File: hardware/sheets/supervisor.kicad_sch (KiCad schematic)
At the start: 20 parts, among them J1 QSPI_FLASH, J2 USB_HOST, J3 POST_HEX, J4 CONSOLE, J5 SWD, U1 RP2040, Y1 12MHz

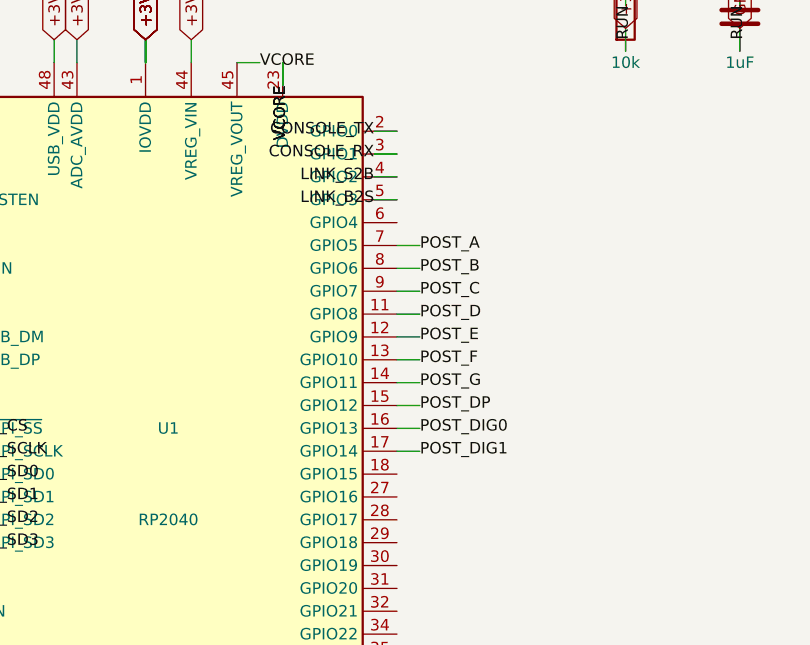
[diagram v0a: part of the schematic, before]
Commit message: Fix all medium design-review findings (M1-M8)
- M1: Supervisor link moved to GPIO4/5 (real UART1 pair); POST -> GPIO6-15
- M2: CNT_RUN = LD0.LD1.LD2 gates every '163 CEP (load-cascade hazard)
- M3: ~WR / IO-M pruned to cpu_core-internal; DRQ2/3 pulled + noted;
  doc S5.2 "as built: 48/48" + S16 updated
- M4: true XT-IDE rev-2 map (A0<->A3 swap): data 0x300, latch 0x301,
  CS1 0x307/0x30F, drive DA0 = bus A3 - matches XTIDE UB "rev 2" type
- M5: COM4 -> bus IRQ2 line (IRQ9 via AT redirect); IRQ10/11/14/15 marked
  off-header; ~REFRESH added to mxbus ISA_CTRL; questions-sidecar superseded
- M6: card_isatest clock tree on unswitched V5RAW (spec S8)
- M7: card_isatest IRQ2-8/DRQ1-3 idle pull-downs (spec S4/S9)
- M8: com_port JP1 selects 16550 RX source (DB9 vs TTL console); 5V note

Rebuilt motherboard + cards; structural ERC = 0; netlist-verified.
Fix log in hardware/notes/design-review-2026-07-03.md (batch 3).

Co-Authored-By: Claude Fable 5 <noreply@anthropic.com>
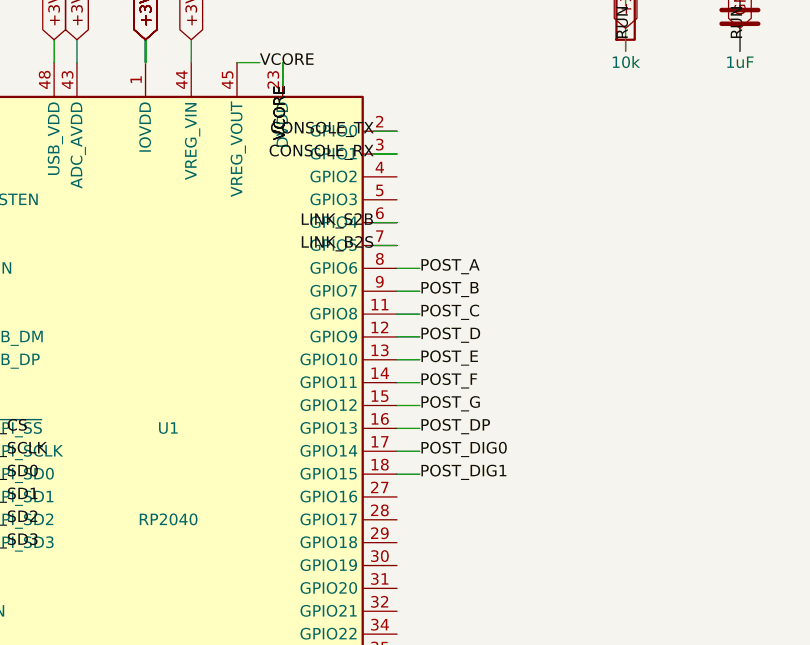
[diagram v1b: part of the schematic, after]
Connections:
- net LINK_B2S: now also U1.7 (GPIO5); no longer U1.5 (GPIO3)
- net LINK_S2B: now also U1.6 (GPIO4); no longer U1.4 (GPIO2)
- net POST_A: now also U1.8 (GPIO6); no longer U1.7 (GPIO5)
- net POST_B: now also U1.9 (GPIO7); no longer U1.8 (GPIO6)
- net POST_C: now also U1.11 (GPIO8); no longer U1.9 (GPIO7)
- net POST_D: now also U1.12 (GPIO9); no longer U1.11 (GPIO8)
- net POST_DIG0: now also U1.17 (GPIO14); no longer U1.16 (GPIO13)
- net POST_DIG1: now also U1.18 (GPIO15); no longer U1.17 (GPIO14)
- net POST_DP: now also U1.16 (GPIO13); no longer U1.15 (GPIO12)
- net POST_E: now also U1.13 (GPIO10); no longer U1.12 (GPIO9)
- net POST_F: now also U1.14 (GPIO11); no longer U1.13 (GPIO10)
- net POST_G: now also U1.15 (GPIO12); no longer U1.14 (GPIO11)
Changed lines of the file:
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@@
-	(wire
-		(pts
-			(xy 203.2 101.6)
-			(xy 205.74 101.6)
-		)
-		(stroke
-			(width 0)
-			(type default)
-		)
-	)
-	(label "POST_A"
-		(at 205.74 101.6 0)
-		(effects
-			(font
-				(size 1.27 1.27)
-			)
-		)
-	)
 	(wire
 		(pts
@@
 		)
 	)
-	(label "POST_B"
+	(label "POST_A"
 		(at 205.74 104.14 0)
 		(effects
@@
 		)
 	)
-	(label "POST_C"
+	(label "POST_B"
 		(at 205.74 106.68 0)
 		(effects
@@
 		)
 	)
-	(label "POST_D"
+	(label "POST_C"
 		(at 205.74 109.22 0)
 		(effects
@@
 		)
 	)
-	(label "POST_E"
+	(label "POST_D"
 		(at 205.74 111.76 0)
 		(effects
@@
 		)
 	)
-	(label "POST_F"
+	(label "POST_E"
 		(at 205.74 114.3 0)
 		(effects
@@
 		)
 	)
-	(label "POST_G"
+	(label "POST_F"
 		(at 205.74 116.84 0)
 		(effects
@@
 		)
 	)
-	(label "POST_DP"
+	(label "POST_G"
 		(at 205.74 119.38 0)
 		(effects
@@
 		)
 	)
-	(label "POST_DIG0"
+	(label "POST_DP"
 		(at 205.74 121.92 0)
 		(effects
@@
 		)
 	)
+	(label "POST_DIG0"
+		(at 205.74 124.46 0)
+		(effects
+			(font
+				(size 1.27 1.27)
+			)
+		)
+	)
+	(wire
+		(pts
+			(xy 203.2 127)
+			(xy 205.74 127)
+		)
+		(stroke
+			(width 0)
+			(type default)
+		)
+	)
 	(label "POST_DIG1"
-		(at 205.74 124.46 0)
+		(at 205.74 127 0)
 		(effects
 			(font
@@
 	(wire
 		(pts
-			(xy 203.2 93.98)
-			(xy 200.66 93.98)
+			(xy 203.2 99.06)
+			(xy 200.66 99.06)
 		)
 		(stroke
@@
 	)
 	(label "LINK_S2B"
-		(at 200.66 93.98 180)
-		(effects
-			(font
-				(size 1.27 1.27)
-			)
-		)
-	)
-	(wire
-		(pts
-			(xy 203.2 96.52)
-			(xy 200.66 96.52)
+		(at 200.66 99.06 180)
+		(effects
+			(font
+				(size 1.27 1.27)
+			)
+		)
+	)
+	(wire
+		(pts
+			(xy 203.2 101.6)
+			(xy 200.66 101.6)
 		)
 		(stroke
@@
 	)
 	(label "LINK_B2S"
-		(at 200.66 96.52 180)
+		(at 200.66 101.6 180)
 		(effects
 			(font
@@
 		(instances
 			(project "mini-xt"
-				(path "/ccbe75bb-9744-49b2-888c-84927206f4cb/4048b6e1-cd1b-4deb-bfe0-8efa00e539cf"
+				(path "/9d1a32b9-fdc3-4ebf-878d-e57919a1b88e/45ccf1e3-24fb-43fe-b9e2-8c06fe84f685"
 					(reference "U301")
 					(unit 1)
@@
 		(instances
 			(project "mini-xt"
-				(path "/ccbe75bb-9744-49b2-888c-84927206f4cb/4048b6e1-cd1b-4deb-bfe0-8efa00e539cf"
+				(path "/9d1a32b9-fdc3-4ebf-878d-e57919a1b88e/45ccf1e3-24fb-43fe-b9e2-8c06fe84f685"
 					(reference "Y301")
 					(unit 1)
@@
 		(instances
 			(project "mini-xt"
-				(path "/ccbe75bb-9744-49b2-888c-84927206f4cb/4048b6e1-cd1b-4deb-bfe0-8efa00e539cf"
+				(path "/9d1a32b9-fdc3-4ebf-878d-e57919a1b88e/45ccf1e3-24fb-43fe-b9e2-8c06fe84f685"
 					(reference "C301")
 					(unit 1)
@@
 		(instances
 			(project "mini-xt"
-				(path "/ccbe75bb-9744-49b2-888c-84927206f4cb/4048b6e1-cd1b-4deb-bfe0-8efa00e539cf"
+				(path "/9d1a32b9-fdc3-4ebf-878d-e57919a1b88e/45ccf1e3-24fb-43fe-b9e2-8c06fe84f685"
 					(reference "C302")
 					(unit 1)
@@
 		(instances
 			(project "mini-xt"
-				(path "/ccbe75bb-9744-49b2-888c-84927206f4cb/4048b6e1-cd1b-4deb-bfe0-8efa00e539cf"
+				(path "/9d1a32b9-fdc3-4ebf-878d-e57919a1b88e/45ccf1e3-24fb-43fe-b9e2-8c06fe84f685"
 					(reference "R301")
 					(unit 1)
@@
 		(instances
 			(project "mini-xt"
-				(path "/ccbe75bb-9744-49b2-888c-84927206f4cb/4048b6e1-cd1b-4deb-bfe0-8efa00e539cf"
+				(path "/9d1a32b9-fdc3-4ebf-878d-e57919a1b88e/45ccf1e3-24fb-43fe-b9e2-8c06fe84f685"
 					(reference "C303")
 					(unit 1)
@@
 		(instances
 			(project "mini-xt"
-				(path "/ccbe75bb-9744-49b2-888c-84927206f4cb/4048b6e1-cd1b-4deb-bfe0-8efa00e539cf"
+				(path "/9d1a32b9-fdc3-4ebf-878d-e57919a1b88e/45ccf1e3-24fb-43fe-b9e2-8c06fe84f685"
 					(reference "J301")
 					(unit 1)
@@
 		(instances
 			(project "mini-xt"
-				(path "/ccbe75bb-9744-49b2-888c-84927206f4cb/4048b6e1-cd1b-4deb-bfe0-8efa00e539cf"
+				(path "/9d1a32b9-fdc3-4ebf-878d-e57919a1b88e/45ccf1e3-24fb-43fe-b9e2-8c06fe84f685"
 					(reference "C304")
 					(unit 1)
@@
 		(instances
 			(project "mini-xt"
-				(path "/ccbe75bb-9744-49b2-888c-84927206f4cb/4048b6e1-cd1b-4deb-bfe0-8efa00e539cf"
+				(path "/9d1a32b9-fdc3-4ebf-878d-e57919a1b88e/45ccf1e3-24fb-43fe-b9e2-8c06fe84f685"
 					(reference "J302")
 					(unit 1)
@@
 		(instances
 			(project "mini-xt"
-				(path "/ccbe75bb-9744-49b2-888c-84927206f4cb/4048b6e1-cd1b-4deb-bfe0-8efa00e539cf"
+				(path "/9d1a32b9-fdc3-4ebf-878d-e57919a1b88e/45ccf1e3-24fb-43fe-b9e2-8c06fe84f685"
 					(reference "J303")
 					(unit 1)
@@
 		(instances
 			(project "mini-xt"
-				(path "/ccbe75bb-9744-49b2-888c-84927206f4cb/4048b6e1-cd1b-4deb-bfe0-8efa00e539cf"
+				(path "/9d1a32b9-fdc3-4ebf-878d-e57919a1b88e/45ccf1e3-24fb-43fe-b9e2-8c06fe84f685"
 					(reference "J304")
 					(unit 1)
@@
 		(instances
 			(project "mini-xt"
-				(path "/ccbe75bb-9744-49b2-888c-84927206f4cb/4048b6e1-cd1b-4deb-bfe0-8efa00e539cf"
+				(path "/9d1a32b9-fdc3-4ebf-878d-e57919a1b88e/45ccf1e3-24fb-43fe-b9e2-8c06fe84f685"
 					(reference "J305")
 					(unit 1)
@@
 		(instances
 			(project "mini-xt"
-				(path "/ccbe75bb-9744-49b2-888c-84927206f4cb/4048b6e1-cd1b-4deb-bfe0-8efa00e539cf"
+				(path "/9d1a32b9-fdc3-4ebf-878d-e57919a1b88e/45ccf1e3-24fb-43fe-b9e2-8c06fe84f685"
 					(reference "C305")
 					(unit 1)
@@
 		(instances
 			(project "mini-xt"
-				(path "/ccbe75bb-9744-49b2-888c-84927206f4cb/4048b6e1-cd1b-4deb-bfe0-8efa00e539cf"
+				(path "/9d1a32b9-fdc3-4ebf-878d-e57919a1b88e/45ccf1e3-24fb-43fe-b9e2-8c06fe84f685"
 					(reference "C306")
 					(unit 1)
@@
 		(instances
 			(project "mini-xt"
-				(path "/ccbe75bb-9744-49b2-888c-84927206f4cb/4048b6e1-cd1b-4deb-bfe0-8efa00e539cf"
+				(path "/9d1a32b9-fdc3-4ebf-878d-e57919a1b88e/45ccf1e3-24fb-43fe-b9e2-8c06fe84f685"
 					(reference "C307")
 					(unit 1)
@@
 		(instances
 			(project "mini-xt"
-				(path "/ccbe75bb-9744-49b2-888c-84927206f4cb/4048b6e1-cd1b-4deb-bfe0-8efa00e539cf"
+				(path "/9d1a32b9-fdc3-4ebf-878d-e57919a1b88e/45ccf1e3-24fb-43fe-b9e2-8c06fe84f685"
 					(reference "C308")
 					(unit 1)
@@
 		(instances
 			(project "mini-xt"
-				(path "/ccbe75bb-9744-49b2-888c-84927206f4cb/4048b6e1-cd1b-4deb-bfe0-8efa00e539cf"
+				(path "/9d1a32b9-fdc3-4ebf-878d-e57919a1b88e/45ccf1e3-24fb-43fe-b9e2-8c06fe84f685"
 					(reference "C309")
 					(unit 1)
@@
 		(instances
 			(project "mini-xt"
-				(path "/ccbe75bb-9744-49b2-888c-84927206f4cb/4048b6e1-cd1b-4deb-bfe0-8efa00e539cf"
+				(path "/9d1a32b9-fdc3-4ebf-878d-e57919a1b88e/45ccf1e3-24fb-43fe-b9e2-8c06fe84f685"
 					(reference "C310")
 					(unit 1)
@@
 		(instances
 			(project "mini-xt"
-				(path "/ccbe75bb-9744-49b2-888c-84927206f4cb/4048b6e1-cd1b-4deb-bfe0-8efa00e539cf"
+				(path "/9d1a32b9-fdc3-4ebf-878d-e57919a1b88e/45ccf1e3-24fb-43fe-b9e2-8c06fe84f685"
 					(reference "C311")
 					(unit 1)
@@
 		(instances
 			(project "mini-xt"
-				(path "/ccbe75bb-9744-49b2-888c-84927206f4cb/4048b6e1-cd1b-4deb-bfe0-8efa00e539cf"
+				(path "/9d1a32b9-fdc3-4ebf-878d-e57919a1b88e/45ccf1e3-24fb-43fe-b9e2-8c06fe84f685"
 					(reference "C312")
 					(unit 1)

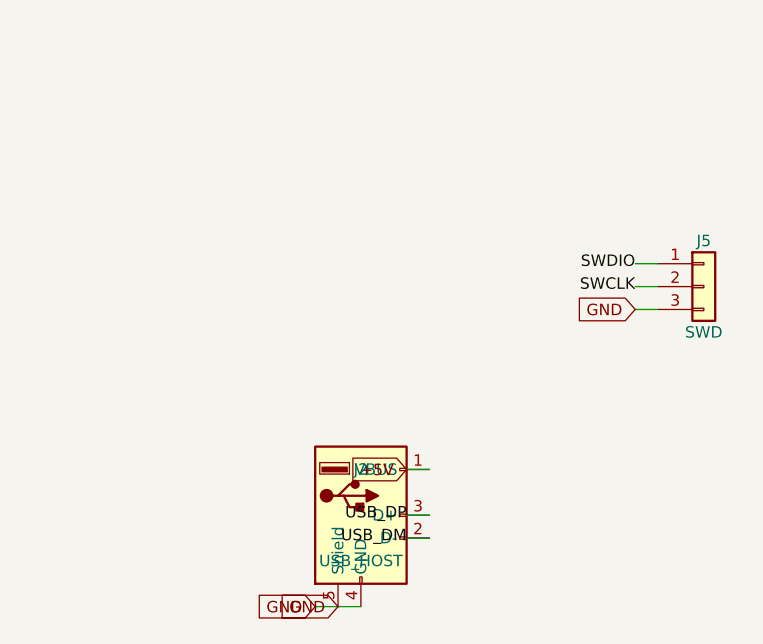
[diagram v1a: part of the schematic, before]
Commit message: Fix all low-severity + toolchain design-review findings
Low:
- LPT IRQ7 via tri-state '125 (NAND-enabled ack pulse) - shareable line
- card_com JP2 IRQ strap follows the base-address strap (was IRQ4-only)
- Supervisor USB-A VBUS fused (500mA polyfuse)
- card_isatest: DUT_PWR_EN moved to the control '595 (addr shifts can't
  glitch DUT power); '165s -> 74HC grade (HCT needs VCC 4.5-5.5V)
- /3 duty comments corrected; U13 marked load-bearing inverting buffer
- RTC AS hold-path bench note; duplicate ~RD stub removed
- mxbus PRIV_DECODE emptied (Y5 never leaves cpu_core)

Toolchain:
- build.py/build_cards return real exit codes, failing on structural ERC
  (endpoint_off_grid/unconnected_wire_endpoint/multiple_net_names) or a
  failed netlist export
- KiCad paths resolved via mxsch.kicad_cli()/kicad_symdir() (env, PATH,
  snap `current`) - no pinned snap revision anywhere
- Deterministic UUIDs (uuid5 title-seed + counter): rebuilds are
  byte-identical (verified); this rewrites every UUID once
- S-expression string escapes now round-trip (parse decodes, dump encodes)
- CLAUDE.md updated to match

The new structural gate immediately caught its own batch's bug (pull row
placed inside card_isatest's J2 pin field) - moved and re-verified.

Co-Authored-By: Claude Fable 5 <noreply@anthropic.com>
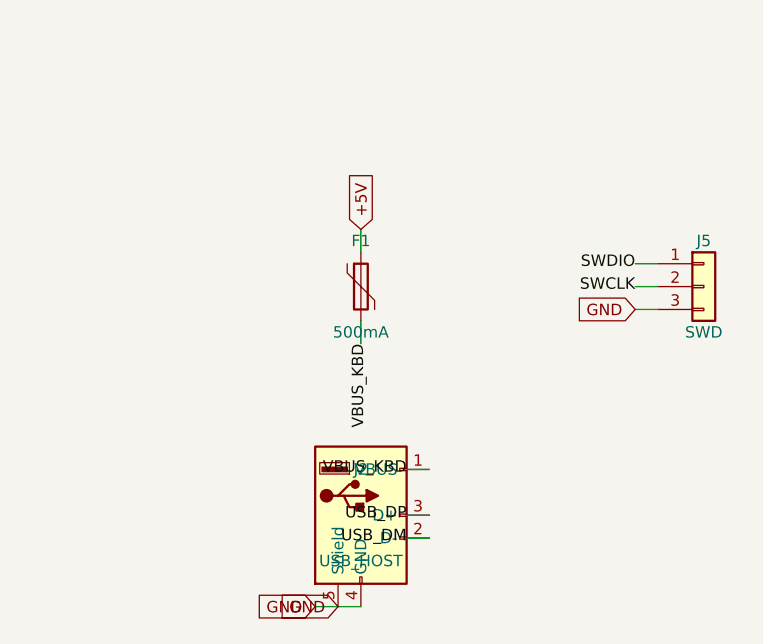
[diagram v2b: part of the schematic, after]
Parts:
- added F1: 500mA, symbol Device:Polyfuse
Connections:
- net +5V: now also F1.1; no longer J2.1 (VBUS)
- new net VBUS_KBD: F1.2, J2.1 (VBUS)
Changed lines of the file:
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@@
+	(wire
+		(pts
+			(xy 63.5 72.39)
+			(xy 63.5 69.85)
+		)
+		(stroke
+			(width 0)
+			(type default)
+		)
+	)
+	(global_label "+5V"
+		(shape input)
+		(at 63.5 69.85 90)
+		(effects
+			(font
+				(size 1.27 1.27)
+			)
+		)
+	)
+	(wire
+		(pts
+			(xy 63.5 80.01)
+			(xy 63.5 82.55)
+		)
+		(stroke
+			(width 0)
+			(type default)
+		)
+	)
+	(label "VBUS_KBD"
+		(at 63.5 82.55 270)
+		(effects
+			(font
+				(size 1.27 1.27)
+			)
+		)
+	)
 	(wire
 		(pts
@@
 		)
 	)
-	(global_label "+5V"
-		(shape input)
+	(label "VBUS_KBD"
 		(at 68.58 96.52 180)
 		(effects
@@
 		(instances
 			(project "mini-xt"
-				(path "/9d1a32b9-fdc3-4ebf-878d-e57919a1b88e/45ccf1e3-24fb-43fe-b9e2-8c06fe84f685"
+				(path "/26736c46-8b40-5460-874f-03596d17270c/e314c42b-162a-53a5-8396-214d4f49fe96"
 					(reference "U301")
 					(unit 1)
@@
 		(instances
 			(project "mini-xt"
-				(path "/9d1a32b9-fdc3-4ebf-878d-e57919a1b88e/45ccf1e3-24fb-43fe-b9e2-8c06fe84f685"
+				(path "/26736c46-8b40-5460-874f-03596d17270c/e314c42b-162a-53a5-8396-214d4f49fe96"
 					(reference "Y301")
 					(unit 1)
@@
 		(instances
 			(project "mini-xt"
-				(path "/9d1a32b9-fdc3-4ebf-878d-e57919a1b88e/45ccf1e3-24fb-43fe-b9e2-8c06fe84f685"
+				(path "/26736c46-8b40-5460-874f-03596d17270c/e314c42b-162a-53a5-8396-214d4f49fe96"
 					(reference "C301")
 					(unit 1)
@@
 		(instances
 			(project "mini-xt"
-				(path "/9d1a32b9-fdc3-4ebf-878d-e57919a1b88e/45ccf1e3-24fb-43fe-b9e2-8c06fe84f685"
+				(path "/26736c46-8b40-5460-874f-03596d17270c/e314c42b-162a-53a5-8396-214d4f49fe96"
 					(reference "C302")
 					(unit 1)
@@
 		(instances
 			(project "mini-xt"
-				(path "/9d1a32b9-fdc3-4ebf-878d-e57919a1b88e/45ccf1e3-24fb-43fe-b9e2-8c06fe84f685"
+				(path "/26736c46-8b40-5460-874f-03596d17270c/e314c42b-162a-53a5-8396-214d4f49fe96"
 					(reference "R301")
 					(unit 1)
@@
 		(instances
 			(project "mini-xt"
-				(path "/9d1a32b9-fdc3-4ebf-878d-e57919a1b88e/45ccf1e3-24fb-43fe-b9e2-8c06fe84f685"
+				(path "/26736c46-8b40-5460-874f-03596d17270c/e314c42b-162a-53a5-8396-214d4f49fe96"
 					(reference "C303")
 					(unit 1)
@@
 		(instances
 			(project "mini-xt"
-				(path "/9d1a32b9-fdc3-4ebf-878d-e57919a1b88e/45ccf1e3-24fb-43fe-b9e2-8c06fe84f685"
+				(path "/26736c46-8b40-5460-874f-03596d17270c/e314c42b-162a-53a5-8396-214d4f49fe96"
 					(reference "J301")
 					(unit 1)
@@
 		(instances
 			(project "mini-xt"
-				(path "/9d1a32b9-fdc3-4ebf-878d-e57919a1b88e/45ccf1e3-24fb-43fe-b9e2-8c06fe84f685"
+				(path "/26736c46-8b40-5460-874f-03596d17270c/e314c42b-162a-53a5-8396-214d4f49fe96"
 					(reference "C304")
 					(unit 1)
@@
 		(instances
 			(project "mini-xt"
-				(path "/9d1a32b9-fdc3-4ebf-878d-e57919a1b88e/45ccf1e3-24fb-43fe-b9e2-8c06fe84f685"
+				(path "/26736c46-8b40-5460-874f-03596d17270c/e314c42b-162a-53a5-8396-214d4f49fe96"
 					(reference "J302")
+					(unit 1)
+				)
+			)
+		)
+	)
+	(symbol
+		(lib_id "Device:Polyfuse")
+		(at 63.5 76.2 0)
+		(unit 1)
+		(exclude_from_sim no)
+		(in_bom yes)
+		(on_board yes)
+		(dnp no)
+		(fields_autoplaced yes)
+		(property "Reference" "F1"
+			(at 63.5 71.12 0)
+			(effects
+				(font
+					(size 1.27 1.27)
+				)
+			)
+		)
+		(property "Value" "500mA"
+			(at 63.5 81.28 0)
+			(effects
+				(font
+					(size 1.27 1.27)
+				)
+			)
+		)
+		(property "Footprint" ""
+			(at 63.5 76.2 0)
+			(effects
+				(font
+					(size 1.27 1.27)
+				)
+				(hide yes)
+			)
+		)
+		(pin "1"
+		)
+		(pin "2"
+		)
+		(instances
+			(project "mini-xt"
+				(path "/26736c46-8b40-5460-874f-03596d17270c/e314c42b-162a-53a5-8396-214d4f49fe96"
+					(reference "F301")
 					(unit 1)
 				)
@@
 		(instances
 			(project "mini-xt"
-				(path "/9d1a32b9-fdc3-4ebf-878d-e57919a1b88e/45ccf1e3-24fb-43fe-b9e2-8c06fe84f685"
+				(path "/26736c46-8b40-5460-874f-03596d17270c/e314c42b-162a-53a5-8396-214d4f49fe96"
 					(reference "J303")
 					(unit 1)
@@
 		(instances
 			(project "mini-xt"
-				(path "/9d1a32b9-fdc3-4ebf-878d-e57919a1b88e/45ccf1e3-24fb-43fe-b9e2-8c06fe84f685"
+				(path "/26736c46-8b40-5460-874f-03596d17270c/e314c42b-162a-53a5-8396-214d4f49fe96"
 					(reference "J304")
 					(unit 1)
@@
 		(instances
 			(project "mini-xt"
-				(path "/9d1a32b9-fdc3-4ebf-878d-e57919a1b88e/45ccf1e3-24fb-43fe-b9e2-8c06fe84f685"
+				(path "/26736c46-8b40-5460-874f-03596d17270c/e314c42b-162a-53a5-8396-214d4f49fe96"
 					(reference "J305")
 					(unit 1)
@@
 		(instances
 			(project "mini-xt"
-				(path "/9d1a32b9-fdc3-4ebf-878d-e57919a1b88e/45ccf1e3-24fb-43fe-b9e2-8c06fe84f685"
+				(path "/26736c46-8b40-5460-874f-03596d17270c/e314c42b-162a-53a5-8396-214d4f49fe96"
 					(reference "C305")
 					(unit 1)
@@
 		(instances
 			(project "mini-xt"
-				(path "/9d1a32b9-fdc3-4ebf-878d-e57919a1b88e/45ccf1e3-24fb-43fe-b9e2-8c06fe84f685"
+				(path "/26736c46-8b40-5460-874f-03596d17270c/e314c42b-162a-53a5-8396-214d4f49fe96"
 					(reference "C306")
 					(unit 1)
@@
 		(instances
 			(project "mini-xt"
-				(path "/9d1a32b9-fdc3-4ebf-878d-e57919a1b88e/45ccf1e3-24fb-43fe-b9e2-8c06fe84f685"
+				(path "/26736c46-8b40-5460-874f-03596d17270c/e314c42b-162a-53a5-8396-214d4f49fe96"
 					(reference "C307")
 					(unit 1)
@@
 		(instances
 			(project "mini-xt"
-				(path "/9d1a32b9-fdc3-4ebf-878d-e57919a1b88e/45ccf1e3-24fb-43fe-b9e2-8c06fe84f685"
+				(path "/26736c46-8b40-5460-874f-03596d17270c/e314c42b-162a-53a5-8396-214d4f49fe96"
 					(reference "C308")
 					(unit 1)
@@
 		(instances
 			(project "mini-xt"
-				(path "/9d1a32b9-fdc3-4ebf-878d-e57919a1b88e/45ccf1e3-24fb-43fe-b9e2-8c06fe84f685"
+				(path "/26736c46-8b40-5460-874f-03596d17270c/e314c42b-162a-53a5-8396-214d4f49fe96"
 					(reference "C309")
 					(unit 1)
@@
 		(instances
 			(project "mini-xt"
-				(path "/9d1a32b9-fdc3-4ebf-878d-e57919a1b88e/45ccf1e3-24fb-43fe-b9e2-8c06fe84f685"
+				(path "/26736c46-8b40-5460-874f-03596d17270c/e314c42b-162a-53a5-8396-214d4f49fe96"
 					(reference "C310")
 					(unit 1)
@@
 		(instances
 			(project "mini-xt"
-				(path "/9d1a32b9-fdc3-4ebf-878d-e57919a1b88e/45ccf1e3-24fb-43fe-b9e2-8c06fe84f685"
+				(path "/26736c46-8b40-5460-874f-03596d17270c/e314c42b-162a-53a5-8396-214d4f49fe96"
 					(reference "C311")
 					(unit 1)
@@
 		(instances
 			(project "mini-xt"
-				(path "/9d1a32b9-fdc3-4ebf-878d-e57919a1b88e/45ccf1e3-24fb-43fe-b9e2-8c06fe84f685"
+				(path "/26736c46-8b40-5460-874f-03596d17270c/e314c42b-162a-53a5-8396-214d4f49fe96"
 					(reference "C312")
 					(unit 1)
